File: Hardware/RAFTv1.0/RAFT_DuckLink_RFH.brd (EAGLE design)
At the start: 73.7 x 83.8 mm, 145 parts, among them J1 AMPHENOL_132134, J2 AMPHENOL_132134, J4 Micro-USB, J5 132134-15, J6 S2B-PH-K-S(LF)(SN), J8 POWER_JACK, Q1 SIA817EDJ, Q2 SI7288DP, Q4 SI7288DP, U1 SX1276, U10 PE4259, U2 MAX2771ETI+, U3 ESP32-D0WD, U4 W25Q16BVSSIG, U5 INTERFACE-CP2102-GMR(QFN28), U6 PE4259, U7 SP0503BAHT, U8 BQ24650RVAR, U9 TPS63070RNMT, Y1 32.768kHz

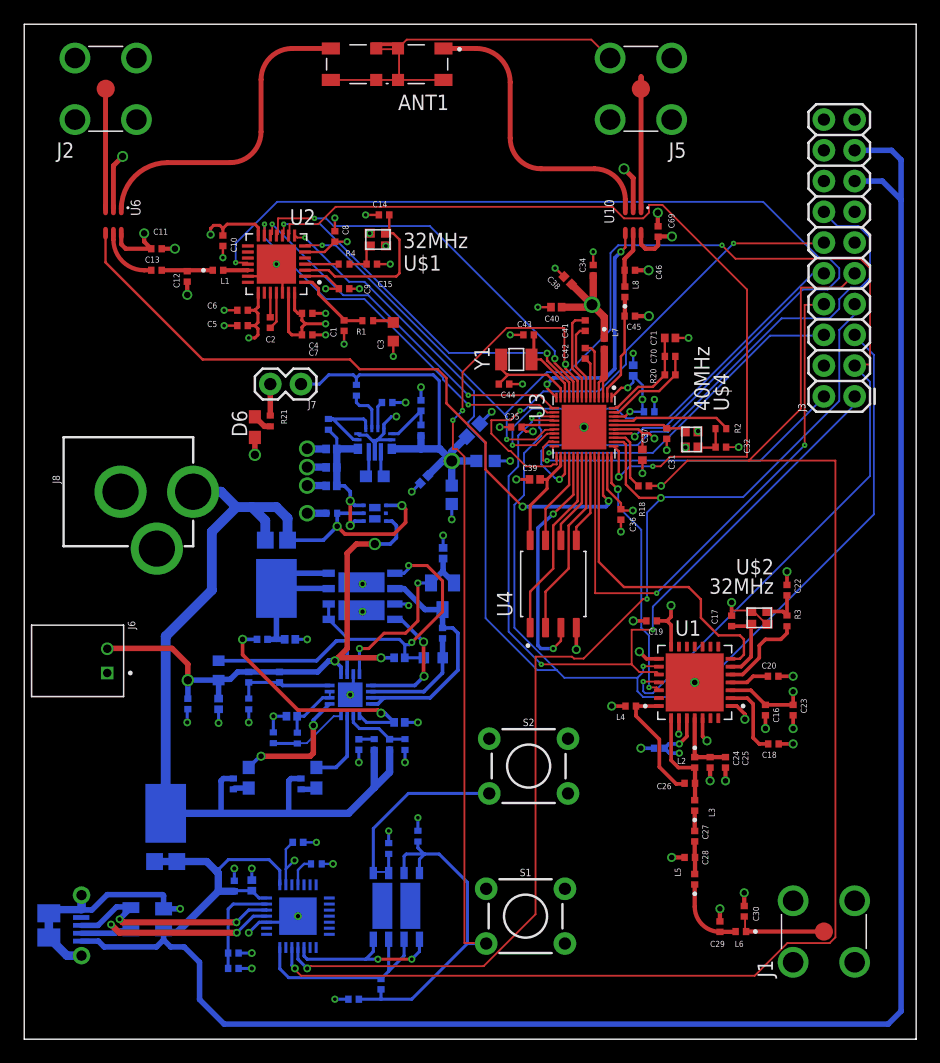
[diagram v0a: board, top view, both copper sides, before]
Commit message: nearly completed board routing. updated gitignore
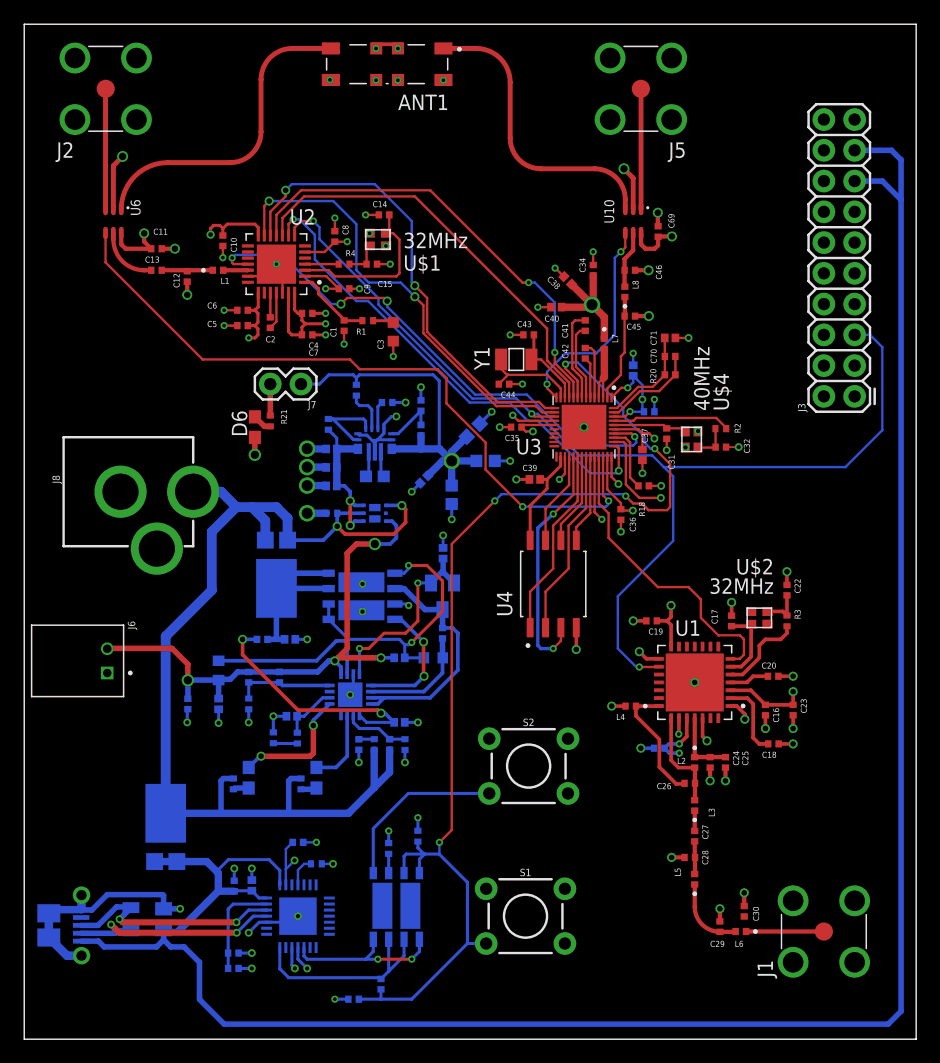
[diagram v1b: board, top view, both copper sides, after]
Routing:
- net U0TXD: track 124.7 -> 2.84 mm
- net SPI_MOSI: track 116.5 -> 0.00 mm, vias 4 -> 0
- net U0RXD: track 98.5 -> 9.80 mm, vias 3 -> 2
- net SPI_MISO: track 65.0 -> 3.62 mm, vias 3 -> 1
- net GPIO17: track 46.8 -> 2.06 mm
- net GPIO16: track 42.6 -> 0.00 mm, vias 2 -> 0
- net GPIO4: track 46.9 -> 5.42 mm, vias 2 -> 1
- net GPIO15: track 37.0 -> 0.00 mm, vias 1 -> 0
- net GPS_SHDN: track 81.2 -> 44.9 mm, vias 2 -> 4
- net GND: track 173.5 -> 137.5 mm, vias 93 -> 99
- net SPI_CLK: track 124.1 -> 92.8 mm
- net GPS_CS: track 71.3 -> 40.7 mm
- net GPIO3: track 27.7 -> 0.00 mm, vias 1 -> 0
- net GPIO0: track 27.6 -> 0.00 mm, vias 1 -> 0
- net SX_CS: track 21.3 -> 2.48 mm, vias 2 -> 1
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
